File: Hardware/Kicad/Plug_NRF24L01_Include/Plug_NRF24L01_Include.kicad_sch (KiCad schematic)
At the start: 55 parts, among them J1 Conn_01x07_Socket, J2 Conn_02x07_Odd_Even, Q1 2N7002, Q2 2N7002, Q3 2N7002, Q4 2N7002, Q5 2N7002, SW2 SW_SPST, U1 STM32L412KBTx, U2 MIC5219-3.3YMM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

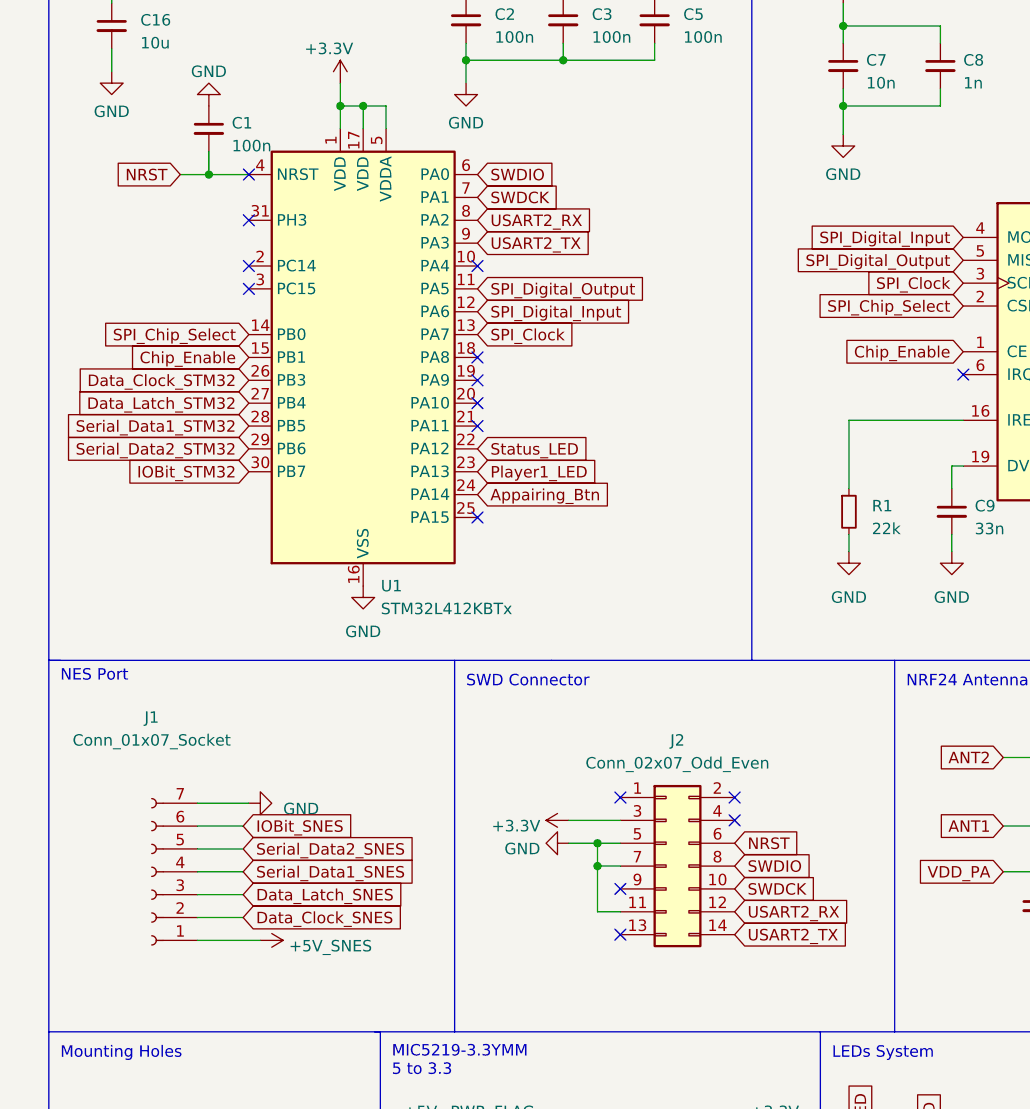
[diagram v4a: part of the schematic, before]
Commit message: Updated Plug_NRF24L01_Include (V2.1) - Schematic & PCB & Image
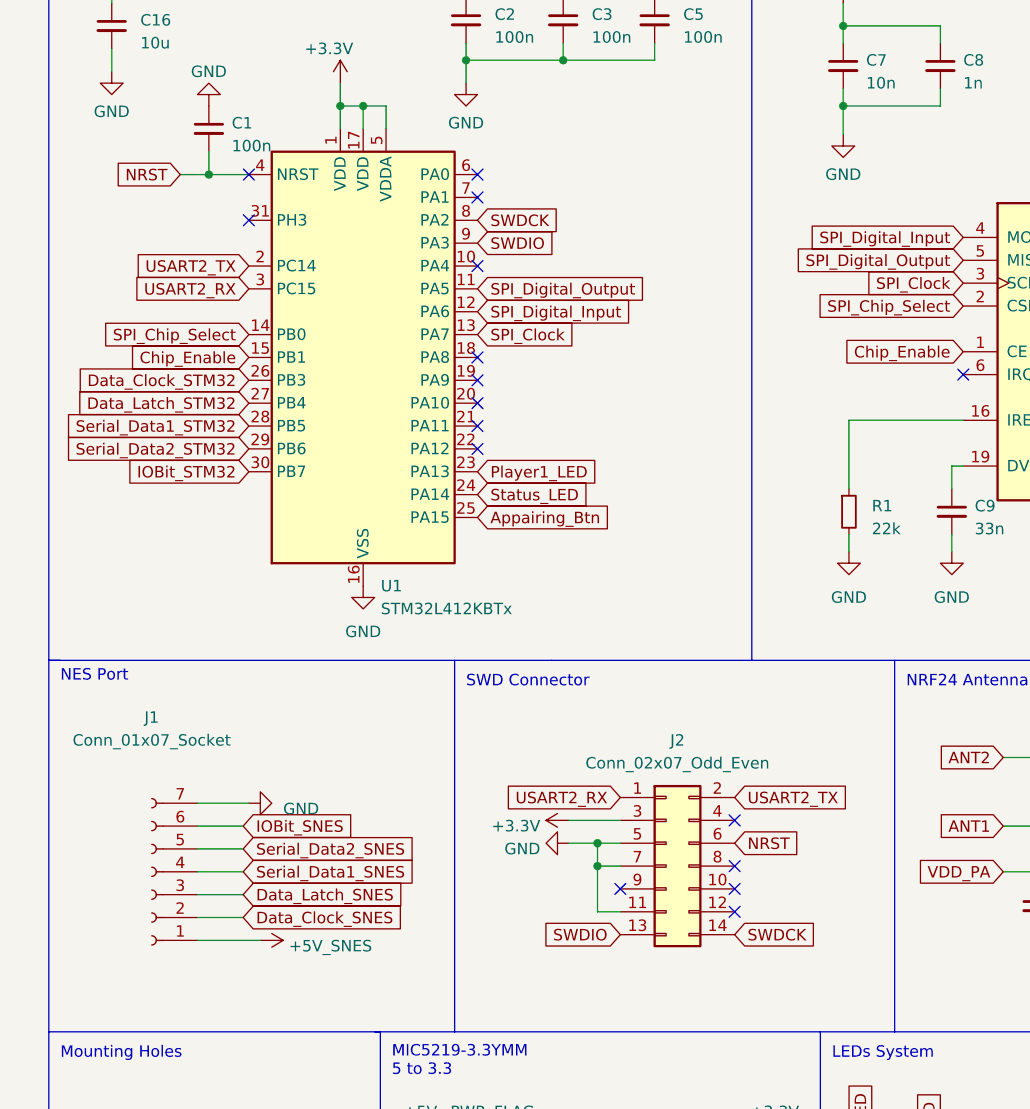
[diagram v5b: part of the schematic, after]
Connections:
- net Appairing_Btn: now also U1.25 (PA15); no longer U1.24 (PA14)
- net SWDCK: now also J2.14 (Pin_14), U1.8 (PA2); no longer J2.10 (Pin_10), U1.7 (PA1)
- net SWDIO: now also J2.13 (Pin_13), U1.9 (PA3); no longer J2.8 (Pin_8), U1.6 (PA0)
- net Status_LED: now also U1.24 (PA14); no longer U1.22 (PA12)
- net USART2_RX: now also J2.1 (Pin_1), U1.3 (PC15); no longer J2.12 (Pin_12), U1.8 (PA2)
- net USART2_TX: now also J2.2 (Pin_2), U1.2 (PC14); no longer J2.14 (Pin_14), U1.9 (PA3)
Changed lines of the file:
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@@
     (title "SNES Wireless Receiver (NRF24L01 Include)")
     (date "2023-04-20")
-    (rev "1.1")
+    (rev "2.1")
     (company "ENSEA")
   )
@@
   (junction (at 48.26 35.56) (diameter 0) (color 0 0 0 0)
   )
-  (no_connect (at 76.835 127.635))
-  (no_connect (at 35.56 55.88))
+  (no_connect (at 60.96 73.66))
   (no_connect (at 60.96 53.34))
+  (no_connect (at 89.535 125.095))
   (no_connect (at 60.96 66.04))
   (no_connect (at 76.835 122.555))
   (no_connect (at 60.96 71.12))
-  (no_connect (at 35.56 53.34))
+  (no_connect (at 89.535 122.555))
   (no_connect (at 62.865 157.48))
   (no_connect (at 35.56 48.26))
   (no_connect (at 89.535 114.935))
-  (no_connect (at 60.96 81.28))
   (no_connect (at 60.96 68.58))
   (no_connect (at 114.935 65.405))
-  (no_connect (at 76.835 112.395))
-  (no_connect (at 89.535 112.395))
+  (no_connect (at 60.96 45.72))
+  (no_connect (at 60.96 43.18))
+  (no_connect (at 89.535 120.015))
   (no_connect (at 60.96 63.5))
   (no_connect (at 35.56 43.18))
@@
     )
   )
-  (global_label "Appairing_Btn" (shape input) (at 60.96 78.74 0) (fields_autoplaced)
-    (effects (font (size 1.27 1.27)) (justify left))
-    (property "Intersheetrefs" "${INTERSHEET_REFS}" (at 76.8075 78.74 0)
-      (effects (font (size 1.27 1.27)) (justify left) hide)
-    )
-  )
   (global_label "ANT2" (shape input) (at 119.38 107.95 180) (fields_autoplaced)
     (effects (font (size 1.27 1.27)) (justify right))
@@
     )
   )
+  (global_label "SWDCK" (shape input) (at 60.96 48.26 0) (fields_autoplaced)
+    (effects (font (size 1.27 1.27)) (justify left))
+    (property "Intersheetrefs" "${INTERSHEET_REFS}" (at 70.3367 48.26 0)
+      (effects (font (size 1.27 1.27)) (justify left) hide)
+    )
+  )
   (global_label "Data_Latch_STM32" (shape input) (at 35.56 68.58 180) (fields_autoplaced)
     (effects (font (size 1.27 1.27)) (justify right))
@@
     )
   )
+  (global_label "USART2_RX" (shape input) (at 76.835 112.395 180) (fields_autoplaced)
+    (effects (font (size 1.27 1.27)) (justify right))
+    (property "Intersheetrefs" "${INTERSHEET_REFS}" (at 63.4064 112.395 0)
+      (effects (font (size 1.27 1.27)) (justify right) hide)
+    )
+  )
   (global_label "SPI_Digital_Input" (shape input) (at 60.96 58.42 0) (fields_autoplaced)
     (effects (font (size 1.27 1.27)) (justify left))
@@
     )
   )
+  (global_label "USART2_RX" (shape input) (at 35.56 55.88 180) (fields_autoplaced)
+    (effects (font (size 1.27 1.27)) (justify right))
+    (property "Intersheetrefs" "${INTERSHEET_REFS}" (at 22.1314 55.88 0)
+      (effects (font (size 1.27 1.27)) (justify right) hide)
+    )
+  )
   (global_label "NRST" (shape input) (at 27.94 43.18 180) (fields_autoplaced)
     (effects (font (size 1.27 1.27)) (justify right))
@@
     )
   )
+  (global_label "SWDCK" (shape input) (at 89.535 127.635 0) (fields_autoplaced)
+    (effects (font (size 1.27 1.27)) (justify left))
+    (property "Intersheetrefs" "${INTERSHEET_REFS}" (at 98.9117 127.635 0)
+      (effects (font (size 1.27 1.27)) (justify left) hide)
+    )
+  )
   (global_label "Data_Latch_SNES" (shape input) (at 34.925 123.19 0) (fields_autoplaced)
     (effects (font (size 1.27 1.27)) (justify left))
@@
     )
   )
+  (global_label "SWDIO" (shape input) (at 76.835 127.635 180) (fields_autoplaced)
+    (effects (font (size 1.27 1.27)) (justify right))
+    (property "Intersheetrefs" "${INTERSHEET_REFS}" (at 68.063 127.635 0)
+      (effects (font (size 1.27 1.27)) (justify right) hide)
+    )
+  )
   (global_label "SPI_Digital_Input" (shape input) (at 114.935 50.165 180) (fields_autoplaced)
     (effects (font (size 1.27 1.27)) (justify right))
@@
     )
   )
+  (global_label "Status_LED" (shape input) (at 60.96 78.74 0) (fields_autoplaced)
+    (effects (font (size 1.27 1.27)) (justify left))
+    (property "Intersheetrefs" "${INTERSHEET_REFS}" (at 74.2675 78.74 0)
+      (effects (font (size 1.27 1.27)) (justify left) hide)
+    )
+  )
   (global_label "ANT2" (shape input) (at 145.415 60.325 0) (fields_autoplaced)
     (effects (font (size 1.27 1.27)) (justify left))
@@
     )
   )
-  (global_label "USART2_RX" (shape input) (at 60.96 48.26 0) (fields_autoplaced)
-    (effects (font (size 1.27 1.27)) (justify left))
-    (property "Intersheetrefs" "${INTERSHEET_REFS}" (at 74.3886 48.26 0)
-      (effects (font (size 1.27 1.27)) (justify left) hide)
-    )
-  )
   (global_label "ANT1" (shape input) (at 145.415 55.245 0) (fields_autoplaced)
     (effects (font (size 1.27 1.27)) (justify left))
@@
     )
   )
-  (global_label "SWDIO" (shape input) (at 60.96 43.18 0) (fields_autoplaced)
-    (effects (font (size 1.27 1.27)) (justify left))
-    (property "Intersheetrefs" "${INTERSHEET_REFS}" (at 69.732 43.18 0)
+  (global_label "Player1_LED" (shape input) (at 60.96 76.2 0) (fields_autoplaced)
+    (effects (font (size 1.27 1.27)) (justify left))
+    (property "Intersheetrefs" "${INTERSHEET_REFS}" (at 75.4166 76.2 0)
       (effects (font (size 1.27 1.27)) (justify left) hide)
     )
@@
     )
   )
+  (global_label "USART2_TX" (shape input) (at 89.535 112.395 0) (fields_autoplaced)
+    (effects (font (size 1.27 1.27)) (justify left))
+    (property "Intersheetrefs" "${INTERSHEET_REFS}" (at 102.6612 112.395 0)
+      (effects (font (size 1.27 1.27)) (justify left) hide)
+    )
+  )
   (global_label "Player1_LED" (shape input) (at 103.505 157.48 90) (fields_autoplaced)
     (effects (font (size 1.27 1.27)) (justify left))
@@
     )
   )
-  (global_label "USART2_TX" (shape input) (at 60.96 50.8 0) (fields_autoplaced)
-    (effects (font (size 1.27 1.27)) (justify left))
-    (property "Intersheetrefs" "${INTERSHEET_REFS}" (at 74.0862 50.8 0)
-      (effects (font (size 1.27 1.27)) (justify left) hide)
-    )
-  )
   (global_label "RF_Output" (shape input) (at 180.975 115.57 180) (fields_autoplaced)
     (effects (font (size 1.27 1.27)) (justify right))
@@
     )
   )
+  (global_label "USART2_TX" (shape input) (at 35.56 53.34 180) (fields_autoplaced)
+    (effects (font (size 1.27 1.27)) (justify right))
+    (property "Intersheetrefs" "${INTERSHEET_REFS}" (at 22.4338 53.34 0)
+      (effects (font (size 1.27 1.27)) (justify right) hide)
+    )
+  )
   (global_label "Appairing_Btn" (shape input) (at 137.16 166.37 0) (fields_autoplaced)
     (effects (font (size 1.27 1.27)) (justify left))
@@
     )
   )
+  (global_label "Appairing_Btn" (shape input) (at 60.96 81.28 0) (fields_autoplaced)
+    (effects (font (size 1.27 1.27)) (justify left))
+    (property "Intersheetrefs" "${INTERSHEET_REFS}" (at 76.8075 81.28 0)
+      (effects (font (size 1.27 1.27)) (justify left) hide)
+    )
+  )
   (global_label "IOBit_SNES" (shape input) (at 257.81 126.365 0) (fields_autoplaced)
     (effects (font (size 1.27 1.27)) (justify left))
@@
     )
   )
-  (global_label "Player1_LED" (shape input) (at 60.96 76.2 0) (fields_autoplaced)
-    (effects (font (size 1.27 1.27)) (justify left))
-    (property "Intersheetrefs" "${INTERSHEET_REFS}" (at 75.4166 76.2 0)
-      (effects (font (size 1.27 1.27)) (justify left) hide)
-    )
-  )
   (global_label "XC2" (shape input) (at 145.415 75.565 0) (fields_autoplaced)
     (effects (font (size 1.27 1.27)) (justify left))
@@
     )
   )
-  (global_label "SWDCK" (shape input) (at 60.96 45.72 0) (fields_autoplaced)
-    (effects (font (size 1.27 1.27)) (justify left))
-    (property "Intersheetrefs" "${INTERSHEET_REFS}" (at 70.3367 45.72 0)
-      (effects (font (size 1.27 1.27)) (justify left) hide)
-    )
-  )
   (global_label "RF_Output" (shape input) (at 151.13 107.95 0) (fields_autoplaced)
     (effects (font (size 1.27 1.27)) (justify left))
@@
     )
   )
+  (global_label "SWDIO" (shape input) (at 60.96 50.8 0) (fields_autoplaced)
+    (effects (font (size 1.27 1.27)) (justify left))
+    (property "Intersheetrefs" "${INTERSHEET_REFS}" (at 69.732 50.8 0)
+      (effects (font (size 1.27 1.27)) (justify left) hide)
+    )
+  )
   (global_label "Data_Clock_SNES" (shape input) (at 257.175 37.465 0) (fields_autoplaced)
     (effects (font (size 1.27 1.27)) (justify left))
@@
     )
   )
-  (global_label "USART2_TX" (shape input) (at 89.535 127.635 0) (fields_autoplaced)
-    (effects (font (size 1.27 1.27)) (justify left))
-    (property "Intersheetrefs" "${INTERSHEET_REFS}" (at 102.6612 127.635 0)
-      (effects (font (size 1.27 1.27)) (justify left) hide)
-    )
-  )
-  (global_label "SWDIO" (shape input) (at 89.535 120.015 0) (fields_autoplaced)
-    (effects (font (size 1.27 1.27)) (justify left))
-    (property "Intersheetrefs" "${INTERSHEET_REFS}" (at 98.307 120.015 0)
-      (effects (font (size 1.27 1.27)) (justify left) hide)
-    )
-  )
-  (global_label "Status_LED" (shape input) (at 60.96 73.66 0) (fields_autoplaced)
-    (effects (font (size 1.27 1.27)) (justify left))
-    (property "Intersheetrefs" "${INTERSHEET_REFS}" (at 74.2675 73.66 0)
-      (effects (font (size 1.27 1.27)) (justify left) hide)
-    )
-  )
   (global_label "IOBit_STM32" (shape input) (at 35.56 76.2 180) (fields_autoplaced)
     (effects (font (size 1.27 1.27)) (justify right))
@@
     )
   )
-  (global_label "USART2_RX" (shape input) (at 89.535 125.095 0) (fields_autoplaced)
-    (effects (font (size 1.27 1.27)) (justify left))
-    (property "Intersheetrefs" "${INTERSHEET_REFS}" (at 102.9636 125.095 0)
-      (effects (font (size 1.27 1.27)) (justify left) hide)
-    )
-  )
   (global_label "SPI_Digital_Output" (shape input) (at 60.96 55.88 0) (fields_autoplaced)
     (effects (font (size 1.27 1.27)) (justify left))
@@
     )
   )
-  (global_label "SWDCK" (shape input) (at 89.535 122.555 0) (fields_autoplaced)
-    (effects (font (size 1.27 1.27)) (justify left))
-    (property "Intersheetrefs" "${INTERSHEET_REFS}" (at 98.9117 122.555 0)
-      (effects (font (size 1.27 1.27)) (justify left) hide)
-    )
-  )
